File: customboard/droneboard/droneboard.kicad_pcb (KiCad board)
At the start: 4 copper layers, 38 x 38 mm, 49 parts, among them J1 Conn_01x04, J3 Conn_01x05_Pin, J4 Conn_01x02_Pin, J7 Conn_01x04_Odd_Even, SW1 SW_Push, SW2 SW_Push, U1 STM32F411CEUx, U3 L78M05CDT, U4 ICM-42688-P, U5 LDK130M33R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

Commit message: usb implementation start
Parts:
- removed J7: Conn_01x04_Odd_Even, Connector_PinHeader_2.54mm:PinHeader_1x04_P2.54mm_Vertical
- added J2: USB_B_Micro, Connector_USB:USB_Micro-B_Molex_47346-0001, F.Cu at (84.8, 101.9)
- moved R9 6.58 mm to (79.8, 92.2), turned to 180 degrees
- moved SW2 6.28 mm to (79.2, 94.8), turned to 0 degrees
- moved D4 4.79 mm to (77.0, 99.8)
- moved R6 4.79 mm to (77.0, 102.5)
- moved D1 4.68 mm to (78.7, 99.7)
- moved R3 4.68 mm to (78.7, 102.6)
- moved SW1 4.66 mm to (79.1, 108.7), turned to 0 degrees
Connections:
- U1 pad 32: /BLUE -> /USB_DM
- U1 pad 33: /YELLOW -> /USB_DP
- U1 pad 34: /SWDIO -> /YELLOW
- U1 pad 37: /SWCLK -> /BLUE
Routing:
- net /USB_DP: track 0.00 -> 12.6 mm
- net /USB_DM: track 0.00 -> 12.5 mm
- net /BLUE: track 17.1 -> 5.49 mm
- net /YELLOW: track 16.0 -> 7.84 mm, vias 2 -> 0
- net /SWCLK: track 6.02 -> 0.00 mm
- net /SWDIO: track 4.98 -> 0.00 mm
- net /RESET1: track 21.9 -> 16.9 mm
- net /GND: track 134.7 -> 131.0 mm
- net /BOOT: track 21.8 -> 22.4 mm
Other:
- board text removed: "3V3"
- board text removed: "CLK"
- board text removed: "DIO"

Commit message: h7 initial
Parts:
- removed U1: STM32F411CEUx, Package_DFN_QFN:QFN-48-1EP_7x7mm_P0.5mm_EP5.6x5.6mm
- added U2: STM32H723VGTx, Package_QFP:LQFP-100_14x14mm_P0.5mm, F.Cu at (70.4, 101.3)
- J4: footprint Connector_JST:JST_XH_B2B-XH-A_1x02_P2.50mm_Vertical -> Connector_PinHeader_1.27mm:PinHeader_1x02_P1.27mm_Vertical
- moved C2 42.5 mm to (33.3, 70.1)
- moved C22 42.5 mm to (33.4, 65.8)
- moved C21 42.5 mm to (41.3, 68.1)
- moved C23 42.5 mm to (33.5, 68.1)
- moved U4 42.5 mm to (37.4, 72.6)
- moved C4 42.5 mm to (39.6, 70.2)
- moved U5 42.5 mm to (37.0, 66.9)
- moved C1 42.5 mm to (33.5, 71.9)
- moved C5 37.4 mm to (27.9, 114.5)
- moved C7 37.4 mm to (27.9, 113.4)
- moved C3 37.4 mm to (38.5, 118.8)
- moved C6 37.4 mm to (38.5, 114.7)
- moved D4 33.6 mm to (93.8, 128.9)
- moved R6 33.6 mm to (93.8, 131.7)
- moved D1 33.6 mm to (95.4, 128.9)
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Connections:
- C15 pad 1: Net-(U1-VCAP1) -> unconnected-(C15-Pad1)
- R1 pad 1: Net-(U1-PB2) -> unconnected-(R1-Pad1)
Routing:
- net /GND: track 131.0 -> 0.00 mm, vias 31 -> 0
- net /5V: track 48.2 -> 0.00 mm
- net /VMCU: track 37.2 -> 0.00 mm, vias 5 -> 0
- net /VBATMON: track 32.2 -> 0.00 mm, vias 2 -> 0
- net /VGYRO: track 30.2 -> 0.00 mm, vias 4 -> 0
- net /RX3: track 20.0 -> 0.00 mm
- net /BOOT: track 22.4 -> 2.98 mm, vias 1 -> 0
- net /12V: track 18.9 -> 0.00 mm
- net /RESET1: track 16.9 -> 0.00 mm, vias 1 -> 0
- net /TX3: track 14.9 -> 0.00 mm, vias 1 -> 0
- net /USB_DP: track 12.6 -> 0.00 mm
- net /USB_DM: track 12.5 -> 0.00 mm
- net Net-(U1-PB2): track 9.62 -> 0.00 mm
- net /GREEN: track 7.99 -> 0.00 mm
- net /YELLOW: track 7.84 -> 0.00 mm
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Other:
- board text removed: "5V"
- board text removed: "GN"
- board text removed: "RX"
- board text removed: "TX"

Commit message: h7 routing
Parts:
- removed J2: USB_B_Micro, Connector_USB:USB_Micro-B_Molex_47346-0001
- added C12: 2.2u, Capacitor_SMD:C_0201_0603Metric, F.Cu at (79.1, 96.5)
- added C8: 100n, Capacitor_SMD:C_0201_0603Metric, F.Cu at (77.6, 94.5)
- added J5: USB_C_Receptacle_USB2.0_16P, Connector_USB:USB_C_Receptacle_GCT_USB4110, F.Cu at (85.1, 101.1)
- added R10: 5.1K, Resistor_SMD:R_0201_0603Metric, F.Cu at (79.8, 99.5)
- added R11: 5.1K, Resistor_SMD:R_0201_0603Metric, F.Cu at (79.9, 103.1)
- C1, C23, C25, C4: footprint Capacitor_SMD:C_0603_1608Metric -> Capacitor_SMD:C_0201_0603Metric
- C10: footprint Capacitor_SMD:C_1206_3216Metric -> Capacitor_SMD:C_0402_1005Metric
- C11, C2, C21, C22, C24, C26: footprint Capacitor_SMD:C_0805_2012Metric -> Capacitor_SMD:C_0201_0603Metric
- C15: value 4.7u -> 2.2u; footprint Capacitor_SMD:C_1206_3216Metric -> Capacitor_SMD:C_0201_0603Metric
- C16, C3, C5, C6, C7, C9: footprint Capacitor_SMD:C_0402_1005Metric -> Capacitor_SMD:C_0201_0603Metric
- R7, R8: footprint Resistor_SMD:R_0603_1608Metric -> Resistor_SMD:R_0201_0603Metric
- R9: footprint Resistor_SMD:R_0402_1005Metric -> Resistor_SMD:R_0201_0603Metric
- moved C9 46.1 mm to (76.8, 109.0), turned to 0 degrees
- moved D2 43.8 mm to (74.1, 91.8), turned to 180 degrees
- moved R4 41.8 mm to (71.5, 92.1), turned to 0 degrees
- moved C7 36.3 mm to (64.2, 110.8), turned to -90 degrees
- moved C5 36.3 mm to (60.2, 97.9)
- moved C3 33.7 mm to (61.6, 94.3), turned to 180 degrees
- moved C26 32.3 mm to (61.8, 91.2), turned to 90 degrees
- moved C10 31.1 mm to (60.8, 92.0)
- moved C16 30.2 mm to (60.0, 103.3)
- moved C24 29.8 mm to (67.2, 90.5)
- moved C11 28.9 mm to (61.0, 93.4), turned to 0 degrees
- moved C15 28.3 mm to (74.6, 110.8), turned to -90 degrees
- moved C25 26.5 mm to (61.5, 89.6), turned to 0 degrees
- moved U6 26.4 mm to (64.4, 90.5), turned to 180 degrees
- moved R7 26.3 mm to (64.3, 87.0), turned to 180 degrees
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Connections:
- C15 pad 1: unconnected-(C15-Pad1) -> Net-(C15-Pad1)
- U2 pad 10: Net-(U2-VSS-Pad10) -> /GND
- U2 pad 19: unconnected-(U2-VSSA-Pad19) -> /GND
- U2 pad 26: Net-(U2-VSS-Pad10) -> /GND
- U2 pad 48: unconnected-(U2-VCAP-Pad48) -> Net-(C15-Pad1)
- U2 pad 49: Net-(U2-VSS-Pad10) -> /GND
- U2 pad 70: unconnected-(U2-PA11-Pad70) -> /USB_DM
- U2 pad 71: unconnected-(U2-PA12-Pad71) -> /USB_DP
- U2 pad 73: unconnected-(U2-VCAP-Pad73) -> Net-(C12-Pad1)
- U2 pad 74: Net-(U2-VSS-Pad10) -> /GND
- U2 pad 99: Net-(U2-VSS-Pad10) -> /GND
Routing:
- net /GND: track 0.00 -> 61.8 mm, vias 0 -> 11
- net /VMCU: track 0.00 -> 42.4 mm, vias 0 -> 8
- net /5V: track 0.00 -> 22.7 mm
- net /USB_DP: track 0.00 -> 8.68 mm
- net /USB_DM: track 0.00 -> 8.64 mm
- net /12V: track 0.00 -> 7.54 mm
- net /NOVBUS: track 0.00 -> 6.12 mm
- net /RESET1: track 0.00 -> 2.81 mm
- net Net-(U2-PH0): track 0.00 -> 2.71 mm
- net Net-(U2-PH1): track 0.00 -> 2.67 mm
- net Net-(J5-SBU1): track 0.00 -> 1.61 mm
- net Net-(J5-SBU2): track 0.00 -> 1.58 mm
- net Net-(C12-Pad1): track 0.00 -> 1.55 mm
- net Net-(C15-Pad1): track 0.00 -> 1.50 mm
- net Net-(U6-BP): track 0.00 -> 1.45 mm
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
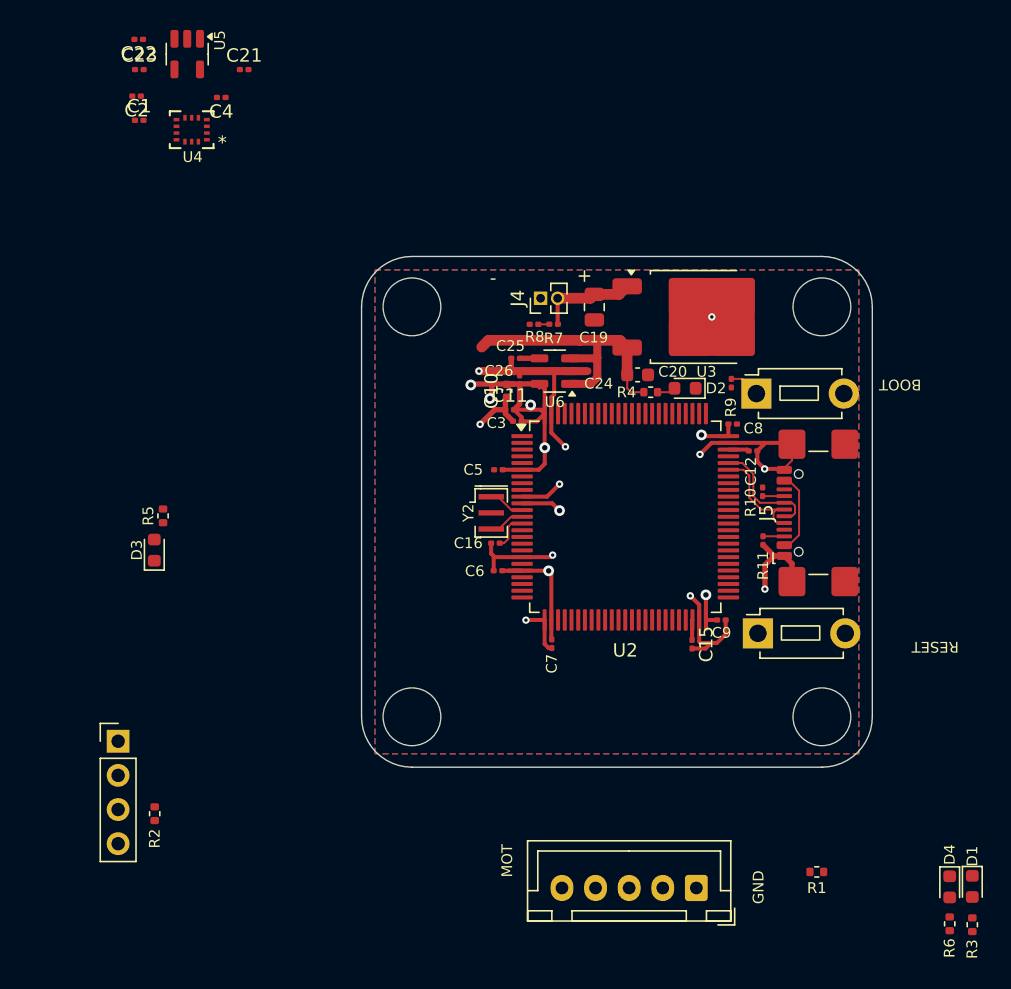
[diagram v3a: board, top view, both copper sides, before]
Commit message: h7 board almost full
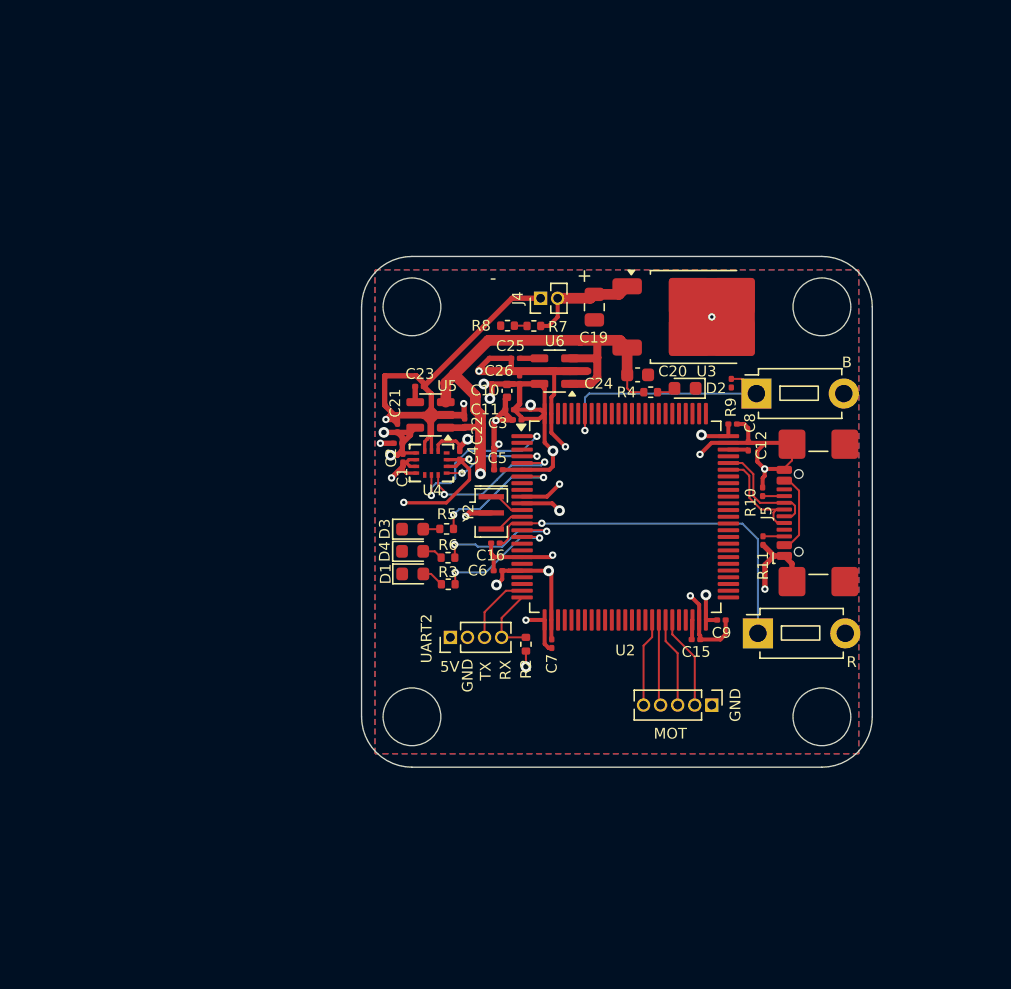
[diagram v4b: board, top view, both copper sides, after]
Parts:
- removed R1: 10K, Resistor_SMD:R_0402_1005Metric
- J1: footprint Connector_PinHeader_2.54mm:PinHeader_1x04_P2.54mm_Vertical -> Connector_PinHeader_1.27mm:PinHeader_1x04_P1.27mm_Vertical
- J3: footprint Connector_JST:JST_XH_B5B-XH-A_1x05_P2.50mm_Vertical -> Connector_PinHeader_1.27mm:PinHeader_1x05_P1.27mm_Vertical
- R7, R8: footprint Resistor_SMD:R_0201_0603Metric -> Resistor_SMD:R_0402_1005Metric
- moved D1 47.7 mm to (53.8, 105.6), turned to 0 degrees
- moved D4 47.1 mm to (53.8, 103.9), turned to 0 degrees
- moved R3 46.5 mm to (56.5, 106.4), turned to 180 degrees
- moved R6 46.2 mm to (56.4, 104.4), turned to 180 degrees
- moved C22 37.4 mm to (57.7, 94.4), turned to 90 degrees
- moved U5 32.4 mm to (55.1, 93.8), turned to 180 degrees
- moved C2 32.3 mm to (52.7, 95.9)
- moved C4 32.0 mm to (57.3, 96.8), turned to 90 degrees
- moved C1 31.9 mm to (53.1, 97.0), turned to 90 degrees
- moved C23 31.5 mm to (54.3, 91.7), turned to 180 degrees
- moved U4 30.6 mm to (55.2, 97.4)
- moved R2 30.4 mm to (62.2, 110.8)
- moved C21 29.0 mm to (52.7, 94.8), turned to 90 degrees
- moved J1 25.9 mm to (56.6, 110.3), turned to 90 degrees
- moved R5 21.1 mm to (56.3, 102.3), turned to 180 degrees
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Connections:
- J1 pad 3: /RX3 -> /U2TX
- J1 pad 4: /TX3 -> /U2RX
- J3 pad 2: /MOTOR0 -> /MOTOR3
- J3 pad 3: /MOTOR1 -> /MOTOR2
- J3 pad 4: /MOTOR2 -> /MOTOR1
- J3 pad 5: /MOTOR3 -> /MOTOR0
- R2 pad 1: /RX3 -> /U2RX
- U2 pad 1: unconnected-(U2-PE2-Pad1) -> /SCK
- U2 pad 15: unconnected-(U2-PC0-Pad15) -> /BLUE
- U2 pad 16: unconnected-(U2-PC1-Pad16) -> /YELLOW
- U2 pad 24: unconnected-(U2-PA2-Pad24) -> /U2TX
- U2 pad 25: unconnected-(U2-PA3-Pad25) -> /U2RX
- U2 pad 4: unconnected-(U2-PE5-Pad4) -> /MISO
- U2 pad 42: unconnected-(U2-PE12-Pad42) -> /MOTOR0
- U2 pad 43: unconnected-(U2-PE13-Pad43) -> /MOTOR1
- U2 pad 44: unconnected-(U2-PE14-Pad44) -> /MOTOR2
- U2 pad 45: unconnected-(U2-PE15-Pad45) -> /MOTOR3
- U2 pad 5: unconnected-(U2-PE6-Pad5) -> /MOSI
- U2 pad 7: unconnected-(U2-PC13-Pad7) -> /GREEN
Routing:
- net /GND: track 61.8 -> 131.5 mm, vias 11 -> 19
- net /5V: track 22.7 -> 51.8 mm, vias 0 -> 1
- net /RESET1: track 2.81 -> 27.9 mm, vias 0 -> 1
- net /BOOT: track 3.48 -> 20.1 mm, vias 0 -> 1
- net /SCK: track 0.00 -> 13.3 mm, vias 0 -> 2
- net /MOSI: track 0.00 -> 11.8 mm, vias 0 -> 2
- net /VGYRO: track 0.00 -> 11.2 mm, vias 0 -> 3
- net /GREEN: track 0.00 -> 10.5 mm, vias 0 -> 2
- net /BLUE: track 0.00 -> 10.2 mm, vias 0 -> 2
- net /YELLOW: track 0.00 -> 9.55 mm, vias 0 -> 2
- net /MISO: track 0.00 -> 8.35 mm, vias 0 -> 2
- net /MOTOR3: track 0.00 -> 7.03 mm
- net /MOTOR2: track 0.00 -> 6.71 mm
- net /MOTOR0: track 0.00 -> 6.60 mm
- net /MOTOR1: track 0.00 -> 6.39 mm
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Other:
- board text added: "5V"
- board text added: "B"
- board text added: "R"
- board text added: "RX"
- board text added: "TX"
- board text added: "UART2"
- board text removed: "BOOT"
- board text removed: "RESET"

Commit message: h7 board work
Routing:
- net /VMCU: track 44.4 -> 45.4 mm
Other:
- board text added: "G"
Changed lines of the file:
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@@
 		(tags "resistor")
 		(property "Reference" "R6"
-			(at 0 0.95 360)
+			(at 0 0.95 0)
 			(layer "F.SilkS")
 			(effects
@@
 		)
 		(property "Value" "1K"
-			(at 0 1.17 360)
+			(at 0 1.17 0)
 			(layer "F.Fab")
 			(effects
@@
 		)
 		(fp_text user "${REFERENCE}"
-			(at 0 0 360)
+			(at 0 0 0)
 			(layer "F.Fab")
 			(effects
@@
 		)
 		(property "Value" "2.2u"
-			(at 0 1.05 360)
+			(at 0 1.05 0)
 			(layer "F.Fab")
 			(effects
@@
 		)
 		(fp_text user "${REFERENCE}"
-			(at 0 -0.68 360)
+			(at 0 -0.68 0)
 			(layer "F.Fab")
 			(effects
@@
 		)
 		(property "Value" "BLUE_LED"
-			(at 0 1.43 360)
+			(at 0 1.43 0)
 			(layer "F.Fab")
 			(effects
@@
 		)
 		(property "Footprint" "LED_SMD:LED_0603_1608Metric"
-			(at 0 0 360)
+			(at 0 0 0)
 			(layer "F.Fab")
 			(hide yes)
@@
 		)
 		(property "Datasheet" ""
-			(at 0 0 360)
+			(at 0 0 0)
 			(layer "F.Fab")
 			(hide yes)
@@
 		)
 		(property "Description" ""
-			(at 0 0 360)
+			(at 0 0 0)
 			(layer "F.Fab")
 			(hide yes)
@@
 		)
 		(fp_text user "${REFERENCE}"
-			(at 0 0 360)
+			(at 0 0 0)
 			(layer "F.Fab")
 			(effects
@@
 		(tags "capacitor")
 		(property "Reference" "C23"
-			(at -0.03 0.93 360)
+			(at -0.03 0.93 0)
 			(layer "F.SilkS")
 			(effects
@@
 		)
 		(property "Value" "10n"
-			(at 0 1.05 360)
+			(at 0 1.05 0)
 			(layer "F.Fab")
 			(effects
@@
 		)
 		(fp_text user "${REFERENCE}"
-			(at 0 -0.68 360)
+			(at 0 -0.68 0)
 			(layer "F.Fab")
 			(effects
@@
 		(tags "capacitor")
 		(property "Reference" "C15"
-			(at 0.01 0.92 360)
+			(at 0.01 0.92 0)
 			(layer "F.SilkS")
 			(effects
@@
 		)
 		(property "Value" "2.2u"
-			(at 0 1.05 360)
+			(at 0 1.05 0)
 			(layer "F.Fab")
 			(effects
@@
 		)
 		(fp_text user "${REFERENCE}"
-			(at 0 -0.68 360)
+			(at 0 -0.68 0)
 			(layer "F.Fab")
 			(effects
@@
 		)
 		(property "Value" "GREEN_LED"
-			(at 0 1.43 360)
+			(at 0 1.43 0)
 			(layer "F.Fab")
 			(effects
@@
 		)
 		(property "Footprint" "LED_SMD:LED_0603_1608Metric"
-			(at 0 0 360)
+			(at 0 0 0)
 			(layer "F.Fab")
 			(hide yes)
@@
 		)
 		(property "Datasheet" ""
-			(at 0 0 360)
+			(at 0 0 0)
 			(layer "F.Fab")
 			(hide yes)
@@
 		)
 		(property "Description" ""
-			(at 0 0 360)
+			(at 0 0 0)
 			(layer "F.Fab")
 			(hide yes)
@@
 		)
 		(fp_text user "${REFERENCE}"
-			(at 0 0 360)
+			(at 0 0 0)
 			(layer "F.Fab")
 			(effects
@@
 		(tags "resistor")
 		(property "Reference" "R3"
-			(at 0.02 0.91 360)
+			(at 0.02 0.91 0)
 			(layer "F.SilkS")
 			(effects
@@
 		)
 		(property "Value" "1K"
-			(at 0 1.17 360)
+			(at 0 1.17 0)
 			(layer "F.Fab")
 			(effects
@@
 		)
 		(fp_text user "${REFERENCE}"
-			(at 0 0 360)
+			(at 0 0 0)
 			(layer "F.Fab")
 			(effects
@@
 		(tags "resistor")
 		(property "Reference" "R2"
-			(at 1.85 0 90)
+			(at 0.02 -1.08 90)
 			(layer "F.SilkS")
 			(effects
@@
 		)
 		(fp_text user "${REFERENCE}"
-			(at 0 1.905 360)
+			(at 0 1.905 0)
 			(layer "F.Fab")
 			(effects
@@
 		(tags "capacitor")
 		(property "Reference" "C7"
-			(at 1.49 0 90)
+			(at 0.11 -1.12 90)
 			(layer "F.SilkS")
 			(effects
@@
 		)
 		(property "Footprint" "footprints:LGA14_2P5X3X0P91_IVS-L"
-			(at 0 0 360)
+			(at 0 0 0)
 			(layer "F.Fab")
 			(hide yes)
@@
 		)
 		(property "Datasheet" "ICM-42688-P"
-			(at 0 0 360)
+			(at 0 0 0)
 			(layer "F.Fab")
 			(hide yes)
@@
 		)
 		(property "Description" ""
-			(at 0 0 360)
+			(at 0 0 0)
 			(layer "F.Fab")
 			(hide yes)
@@
 		)
 		(fp_text user "*"
-			(at -0.9144 -1 360)
+			(at -0.9144 -1 0)
 			(layer "F.Fab")
 			(effects
@@
 		(tags "resistor")
 		(property "Reference" "R5"
-			(at 0 1.1 360)
+			(at 0 1.1 0)
 			(layer "F.SilkS")
 			(effects
@@
 		)
 		(property "Value" "1K"
-			(at 0 1.17 360)
+			(at 0 1.17 0)
 			(layer "F.Fab")
 			(effects
@@
 		)
 		(fp_text user "${REFERENCE}"
-			(at 0 0 360)
+			(at 0 0 0)
 			(layer "F.Fab")
 			(effects
@@
 		(tags "SOT TO_SOT_SMD")
 		(property "Reference" "U5"
-			(at -1.24 2.16 360)
+			(at -1.24 2.16 0)
 			(layer "F.SilkS")
 			(effects
@@
 		)
 		(property "Value" "LDK130M33R"
-			(at 0 2.4 360)
+			(at 0 2.4 0)
 			(layer "F.Fab")
 			(effects
@@
 		)
 		(fp_text user "${REFERENCE}"
-			(at 0 0 360)
+			(at 0 0 0)
 			(layer "F.Fab")
 			(effects
@@
 		)
 		(property "Value" "YELLOW_LED"
-			(at 0 1.43 360)
+			(at 0 1.43 0)
 			(layer "F.Fab")
 			(effects
@@
 		)
 		(property "Footprint" "LED_SMD:LED_0603_1608Metric"
-			(at 0 0 360)
+			(at 0 0 0)
 			(layer "F.Fab")
 			(hide yes)
@@
 		)
 		(property "Datasheet" ""
-			(at 0 0 360)
+			(at 0 0 0)
 			(layer "F.Fab")
 			(hide yes)
@@
 		)
 		(property "Description" ""
-			(at 0 0 360)
+			(at 0 0 0)
 			(layer "F.Fab")
 			(hide yes)
@@
 		)
 		(fp_text user "${REFERENCE}"
-			(at 0 0 360)
+			(at 0 0 0)
 			(layer "F.Fab")
 			(effects
@@
 		)
 		(fp_text user "${REFERENCE}"
-			(at 0 2.54 360)
+			(at 0 2.54 0)
 			(layer "F.Fab")
 			(effects
@@
 	)
 	(gr_text "5V"
-		(at 55.84 113 0)
+		(at 57.07 109.17 90)
 		(layer "F.SilkS")
 		(effects
@@
 		)
 	)
-	(gr_text "GND"
-		(at 58.36 114.44 90)
+	(gr_text "G"
+		(at 58.37 109.23 90)
 		(layer "F.SilkS")
 		(effects
@@
 	)
 	(gr_text "RX"
-		(at 61.18 113.53 90)
+		(at 60.83 109.23 90)
 		(layer "F.SilkS")
 		(effects
@@
 	)
 	(gr_text "TX"
-		(at 59.7 113.56 90)
+		(at 59.61 109.12 90)
 		(layer "F.SilkS")
 		(effects
@@
 	)
 	(segment
-		(start 62.23 111.36)
-		(end 62.23 112.52)
-		(width 0.15)
-		(layer "F.Cu")
-		(net 18)
-	)
-	(segment
 		(start 63.62 93.695)
 		(end 63.235 94.08)
@@
 	)
 	(segment
+		(start 62.23 111.36)
+		(end 61.35 111.36)
+		(width 0.15)
+		(layer "F.Cu")
+		(net 18)
+	)
+	(segment
+		(start 61.35 111.36)
+		(end 60.4 112.31)
+		(width 0.15)
+		(layer "F.Cu")
+		(net 18)
+	)
+	(segment
 		(start 60.94 105.38)
 		(end 61.935 105.38)
@@
 	)
 	(via
-		(at 62.23 112.52)
+		(at 60.4 112.31)
 		(size 0.8)
 		(drill 0.4)
